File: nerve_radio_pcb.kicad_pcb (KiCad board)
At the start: 4 copper layers, 50 x 50 mm, 26 parts, among them J1 BF030-20A-B1-0360-0277-0600-LB, J2 Battery, J3 5V GPIO Breakout, J4 3V SPI Breakout, U1 LMR51430, U2 TXB0104QPWRQ1, U3 XBP9B-DMWT-002

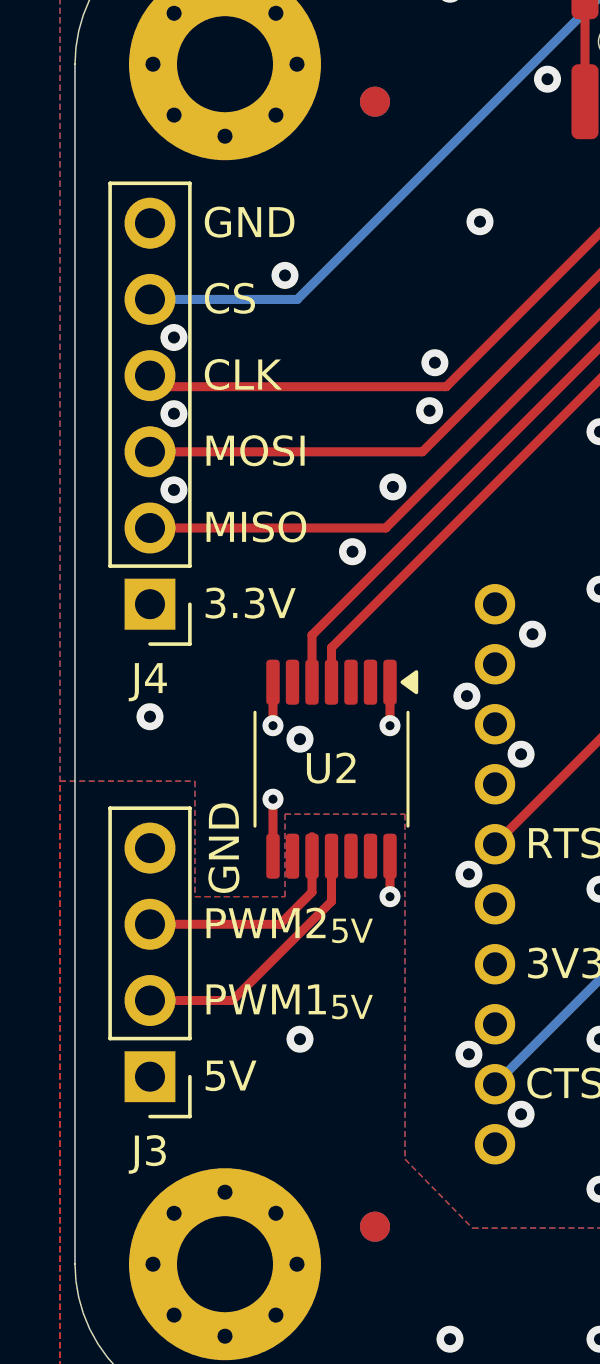
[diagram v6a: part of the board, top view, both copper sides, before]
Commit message: Update for KiCad 9.0 and component library
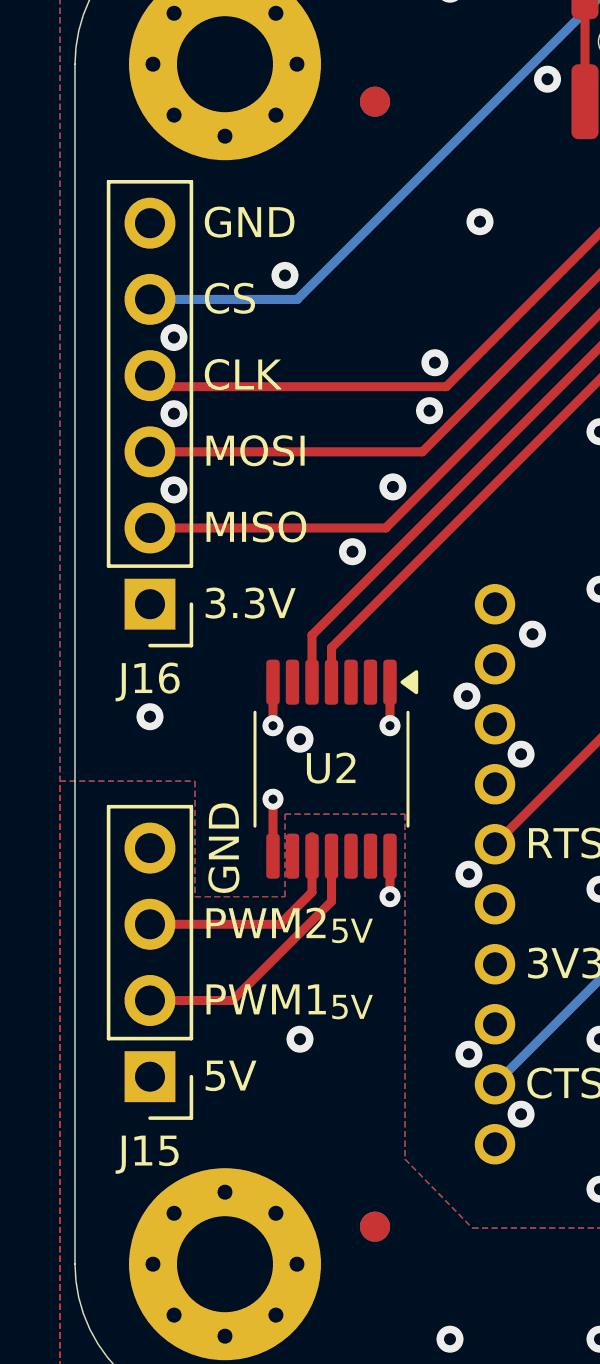
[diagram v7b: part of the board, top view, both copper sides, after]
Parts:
- renumbered J3 to J15, J4 to J16
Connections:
- net /GPIO_2/PWM_2 renamed /GPIO_2/PWM_2/ADC_DRDY

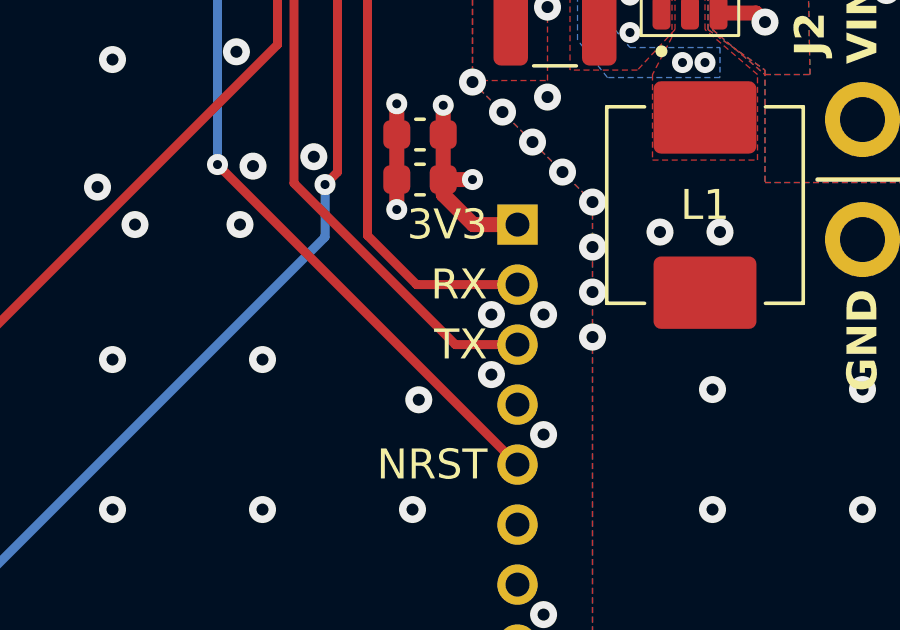
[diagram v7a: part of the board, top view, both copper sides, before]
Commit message: Move UART RX/TX flip to board-to-board connector
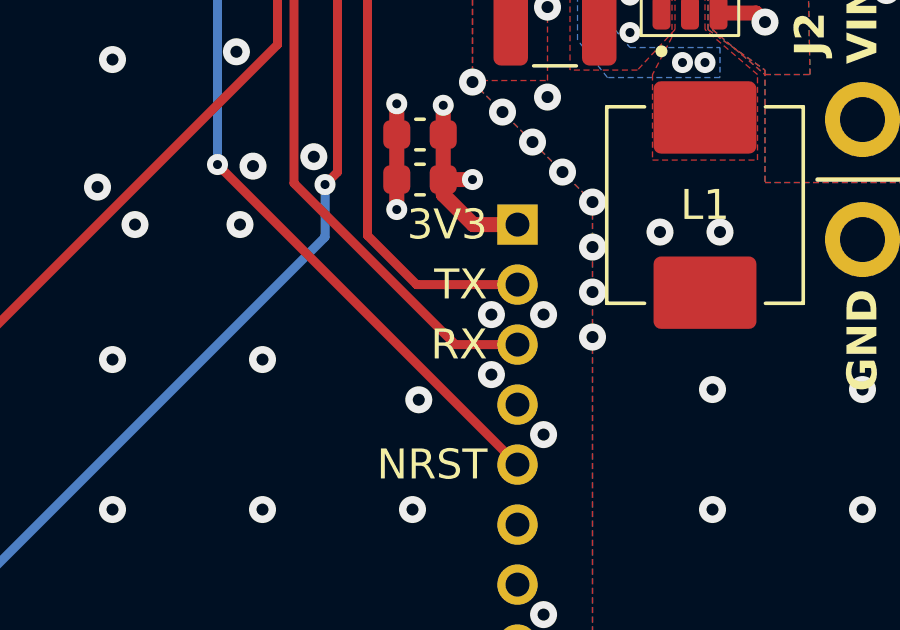
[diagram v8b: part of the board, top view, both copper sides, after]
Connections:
- J1 pad 5: /RADIO_UART_RX -> /RADIO_UART_TX
- J1 pad 7: /RADIO_UART_TX -> /RADIO_UART_RX
- U3 pad 2: /RADIO_UART_RX -> /RADIO_UART_TX
- U3 pad 3: /RADIO_UART_TX -> /RADIO_UART_RX
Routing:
- net /RADIO_UART_TX: track 25.2 -> 22.8 mm
- net /RADIO_UART_RX: track 22.8 -> 25.2 mm
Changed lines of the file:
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@@
 			(layers "F.Cu" "F.Mask" "F.Paste")
 			(roundrect_rratio 0.25)
-			(net 14 "/RADIO_UART_RX")
+			(net 10 "/RADIO_UART_TX")
 			(pintype "passive")
 			(thermal_bridge_angle 45)
@@
 			(layers "F.Cu" "F.Mask" "F.Paste")
 			(roundrect_rratio 0.25)
-			(net 10 "/RADIO_UART_TX")
+			(net 14 "/RADIO_UART_RX")
 			(pintype "passive")
 			(thermal_bridge_angle 45)
@@
 			(layers "*.Cu" "*.Mask")
 			(remove_unused_layers no)
-			(net 14 "/RADIO_UART_RX")
+			(net 10 "/RADIO_UART_TX")
 			(pinfunction "DOUT/DIO13")
 			(pintype "bidirectional")
@@
 			(layers "*.Cu" "*.Mask")
 			(remove_unused_layers no)
-			(net 10 "/RADIO_UART_TX")
+			(net 14 "/RADIO_UART_RX")
 			(pinfunction "DIN/~{CONFIG}/DIO14")
 			(pintype "bidirectional")
@@
 		)
 	)
-	(gr_text "TX"
+	(gr_text "RX"
 		(at 158.5 107 0)
 		(layer "F.SilkS")
@@
 		)
 	)
-	(gr_text "RX"
+	(gr_text "TX"
 		(at 158.5 105 0)
 		(layer "F.SilkS")
@@
 		)
 	)
-	(gr_text "RX"
+	(gr_text "TX"
 		(at 158.5 105 0)
 		(layer "B.SilkS")
@@
 		)
 	)
-	(gr_text "TX"
-		(at 158.5 107 -0)
+	(gr_text "RX"
+		(at 158.5 107 0)
 		(layer "B.SilkS")
 		(effects
@@
 	)
 	(segment
-		(start 152.05 86.7)
-		(end 152.05 101.622056)
-		(width 0.3)
-		(layer "F.Cu")
-		(net 10)
-	)
-	(segment
-		(start 157.429844 107.0019)
-		(end 159.5 107.0019)
+		(start 156.13695 105.0019)
+		(end 159.5 105.0019)
 		(width 0.3)
 		(layer "F.Cu")
@@
 	)
 	(segment
-		(start 152.5 86.25)
-		(end 152.05 86.7)
+		(start 154.5 86.25)
+		(end 154.5 103.36495)
 		(width 0.3)
 		(layer "F.Cu")
@@
 	)
 	(segment
-		(start 152.05 101.622056)
-		(end 157.429844 107.0019)
+		(start 154.5 103.36495)
+		(end 156.13695 105.0019)
 		(width 0.3)
 		(layer "F.Cu")
@@
 	)
 	(segment
-		(start 156.13695 105.0019)
-		(end 159.5 105.0019)
+		(start 152.05 86.7)
+		(end 152.05 101.622056)
 		(width 0.3)
 		(layer "F.Cu")
@@
 	)
 	(segment
-		(start 154.5 86.25)
-		(end 154.5 103.36495)
+		(start 157.429844 107.0019)
+		(end 159.5 107.0019)
 		(width 0.3)
 		(layer "F.Cu")
@@
 	)
 	(segment
-		(start 154.5 103.36495)
-		(end 156.13695 105.0019)
+		(start 152.5 86.25)
+		(end 152.05 86.7)
+		(width 0.3)
+		(layer "F.Cu")
+		(net 14)
+	)
+	(segment
+		(start 152.05 101.622056)
+		(end 157.429844 107.0019)
 		(width 0.3)
 		(layer "F.Cu")
